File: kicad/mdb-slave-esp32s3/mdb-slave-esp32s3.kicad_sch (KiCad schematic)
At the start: 42 parts, among them J1 MDB_Connector, J2 USB_C_Receptacle_USB2.0_16P, J3 Conn_02x11_Odd_Even, SW1 SW_Push, U1 TLP785, U3 ESP32-S3FH4R2, U4 TLP785, U5 LM2594HVM-3.3, Y1 Crystal_GND24

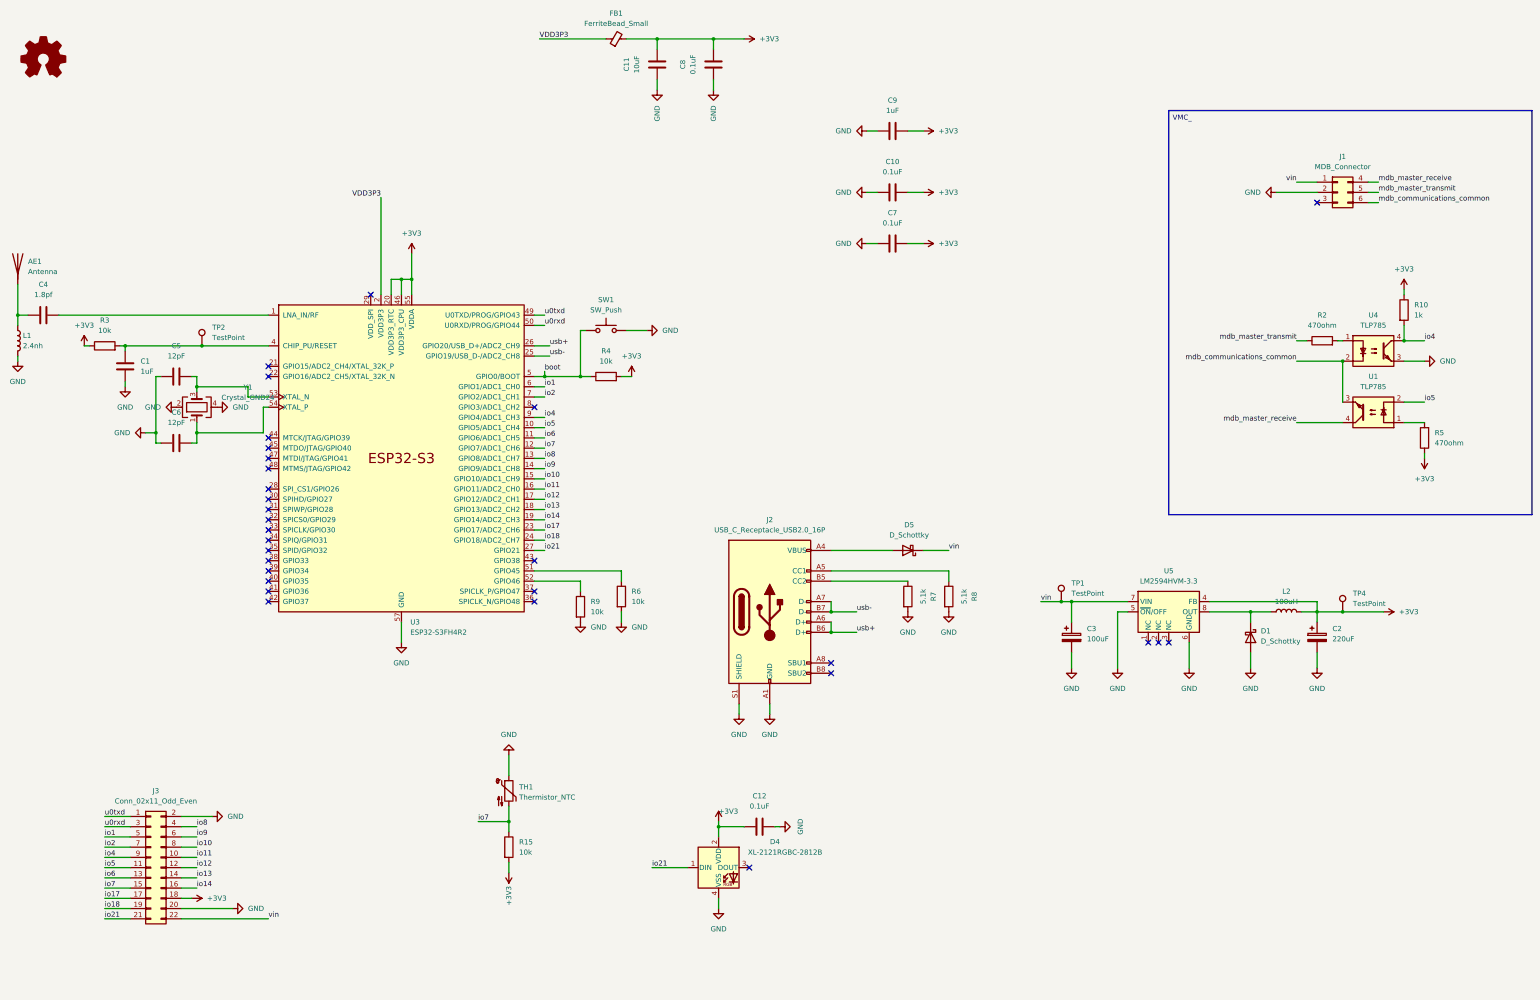
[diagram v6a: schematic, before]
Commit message: mdb-slave-esp32s3 DEX level shifter routing
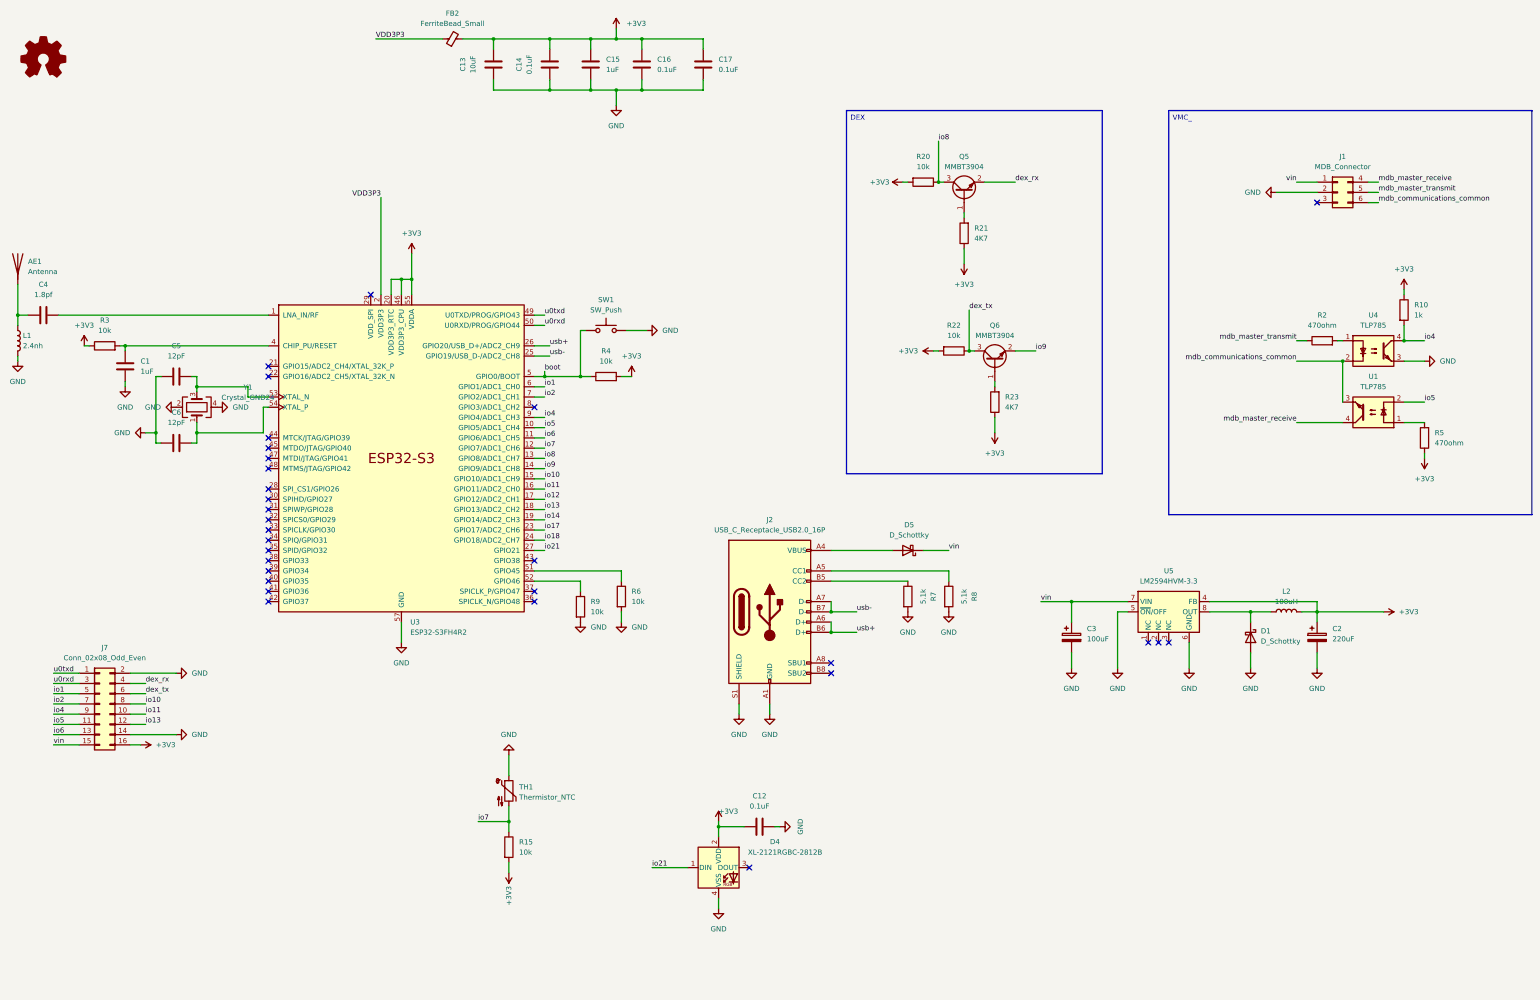
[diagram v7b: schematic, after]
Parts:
- removed C10, C7, C8: 0.1uF, Capacitor_SMD:C_0603_1608Metric, symbol Device:C
- removed C11: 10uF, Capacitor_SMD:C_0603_1608Metric, symbol Device:C
- removed C9: 1uF, Capacitor_SMD:C_0603_1608Metric, symbol Device:C
- removed FB1: FerriteBead_Small, Inductor_SMD:L_0603_1608Metric, symbol Device:FerriteBead_Small
- removed J3: Conn_02x11_Odd_Even, Connector_PinHeader_2.54mm:PinHeader_2x11_P2.54mm_Vertical, symbol Connector_Generic:Conn_02x11_Odd_Even
- removed TP1, TP2, TP4: TestPoint, TestPoint:TestPoint_Pad_D1.0mm, symbol Connector:TestPoint
- added C13: 10uF, Capacitor_SMD:C_0603_1608Metric, symbol Device:C
- added C14, C16, C17: 0.1uF, Capacitor_SMD:C_0603_1608Metric, symbol Device:C
- added C15: 1uF, Capacitor_SMD:C_0603_1608Metric, symbol Device:C
- added FB2: FerriteBead_Small, Inductor_SMD:L_0603_1608Metric, symbol Device:FerriteBead_Small
- added J7: Conn_02x08_Odd_Even, Connector_PinHeader_2.54mm:PinHeader_2x08_P2.54mm_Vertical, symbol Connector_Generic:Conn_02x08_Odd_Even
- added Q5, Q6: MMBT3904, Package_TO_SOT_SMD:SOT-23, symbol Transistor_BJT:MMBT3904
- added R20, R22: 10k, Resistor_SMD:R_0603_1608Metric, symbol Device:R
- added R21, R23: 4K7, Resistor_SMD:R_0603_1608Metric, symbol Device:R
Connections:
- net +3V3: now also C13.2, C14.2, C15.2, C16.1, C17.1, FB2.2, J7.16 (Pin_16), R20.2, R21.1, R22.2, R23.1
- net GND: now also C13.1, C14.1, C15.1, C16.2, C17.2, J7.14 (Pin_14), J7.2 (Pin_2)
- net VDD3P3: now also FB2.1
- net io1: now also J7.5 (Pin_5)
- net io10: now also J7.8 (Pin_8)
- net io11: now also J7.10 (Pin_10)
- net io13: now also J7.12 (Pin_12)
- net io2: now also J7.7 (Pin_7)
- net io4: now also J7.9 (Pin_9)
- net io5: now also J7.11 (Pin_11)
- net io6: now also J7.13 (Pin_13)
- net io8: now also Q5.3 (C), R20.1
- net io9: now also Q6.2 (E)
- net u0rxd: now also J7.3 (Pin_3)
- net u0txd: now also J7.1 (Pin_1)
- net vin: now also J7.15 (Pin_15)
- new net: Q6.1 (B), R23.2
- new net: Q5.1 (B), R21.2
- new net dex_rx: J7.4 (Pin_4), Q5.2 (E)
- new net dex_tx: J7.6 (Pin_6), Q6.3 (C), R22.1

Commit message: Implementing JST socket to i2c and dex
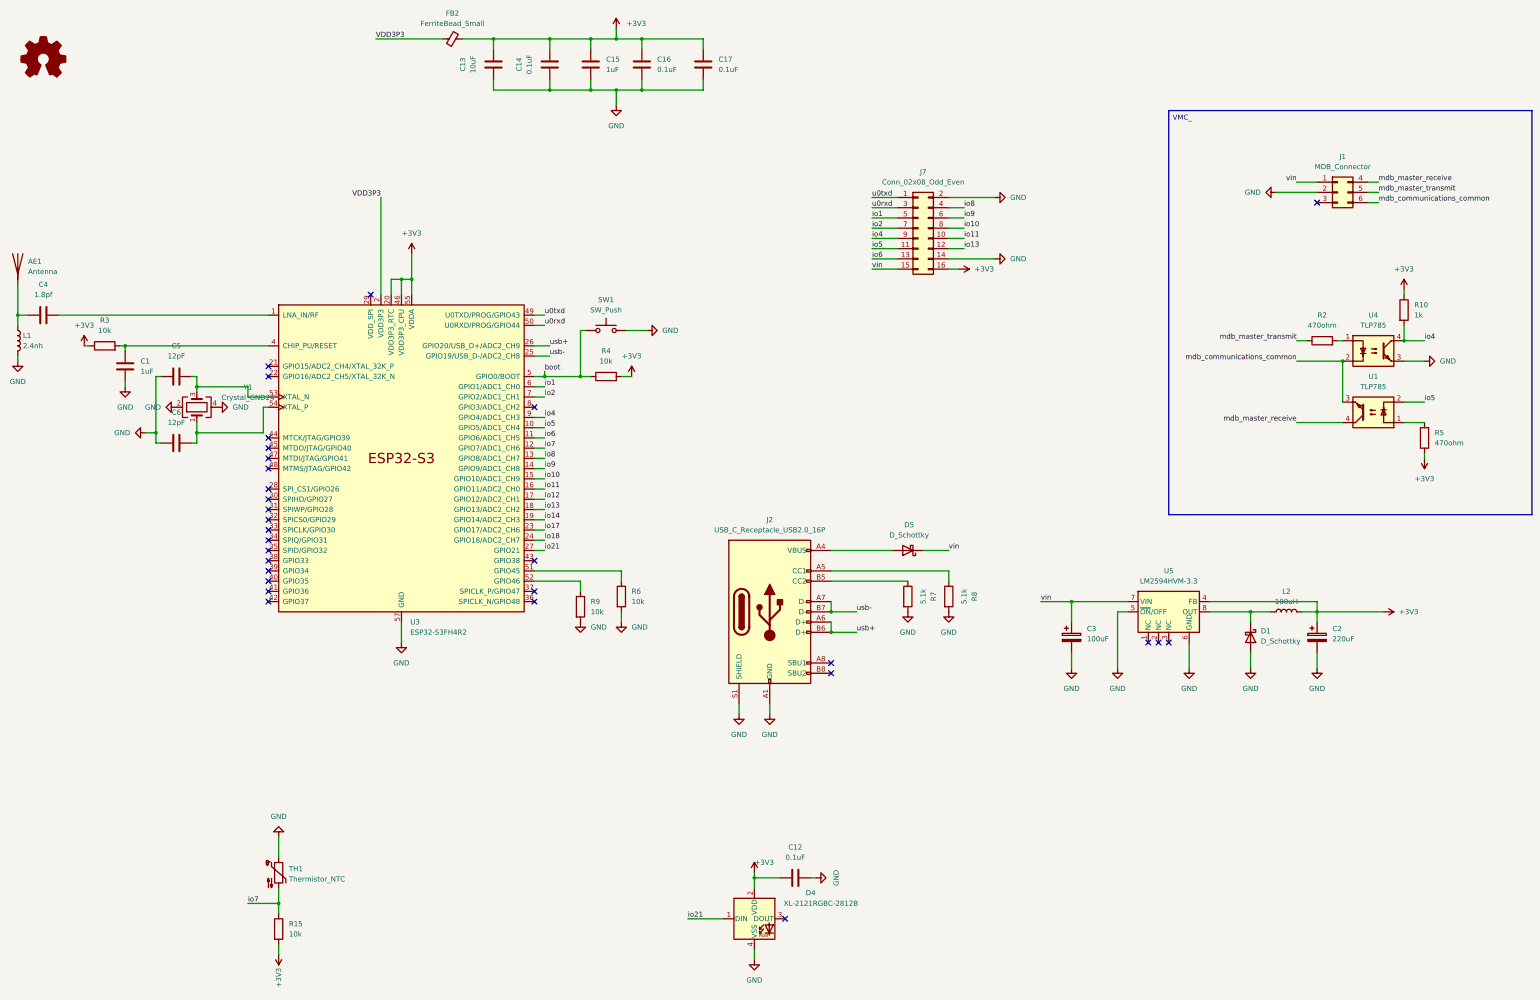
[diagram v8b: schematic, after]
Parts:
- removed Q5, Q6: MMBT3904, Package_TO_SOT_SMD:SOT-23, symbol Transistor_BJT:MMBT3904
- removed R20, R22: 10k, Resistor_SMD:R_0603_1608Metric, symbol Device:R
- removed R21, R23: 4K7, Resistor_SMD:R_0603_1608Metric, symbol Device:R
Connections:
- net dex_rx is gone; now on net io8: J7.4 (Pin_4)
- net dex_tx is gone; now on net io9: J7.6 (Pin_6)
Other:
- moved on the sheet: C12, D4, J7, R15, TH1
